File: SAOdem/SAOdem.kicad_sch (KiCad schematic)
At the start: 1 part, among them U1 SI3018

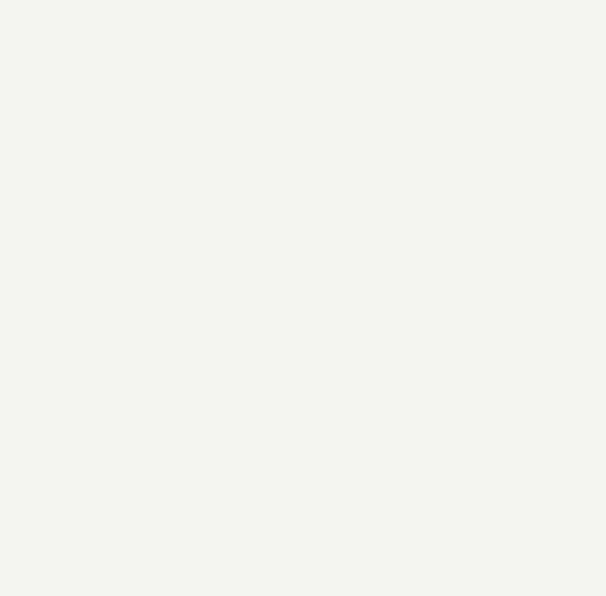
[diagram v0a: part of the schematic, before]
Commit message: Adding Modem chip symbol
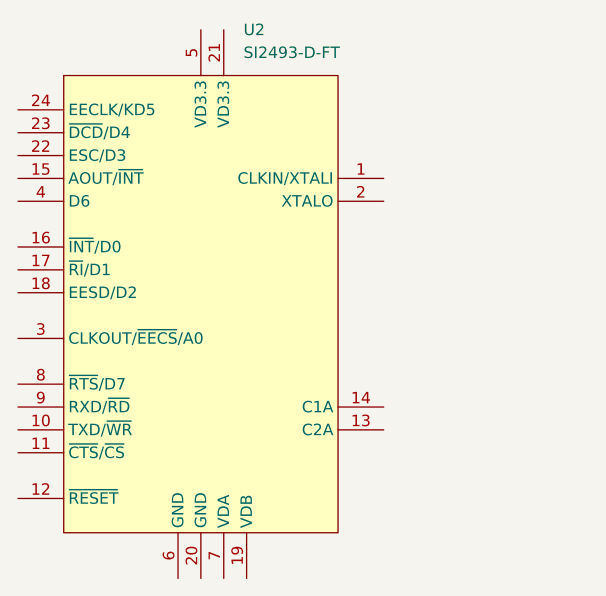
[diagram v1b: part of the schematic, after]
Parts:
- added U2: SI2493-D-FT, Package_SO:TSSOP-24_4.4x6.5mm_P0.5mm, symbol SAOdem:SI2493-D-FT
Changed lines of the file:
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@@
 	(paper "USLetter")
+	(symbol
+		(lib_id "SAOdem:SI2493-D-FT")
+		(at 121.92 82.55 0)
+		(unit 1)
+		(exclude_from_sim no)
+		(in_bom yes)
+		(on_board yes)
+		(dnp no)
+		(fields_autoplaced yes)
+		(property "Reference" "U2"
+			(at 126.6541 52.07 0)
+			(effects
+				(font
+					(size 1.27 1.27)
+				)
+				(justify left)
+			)
+		)
+		(property "Value" "SI2493-D-FT"
+			(at 126.6541 54.61 0)
+			(effects
+				(font
+					(size 1.27 1.27)
+				)
+				(justify left)
+			)
+		)
+		(property "Footprint" "Package_SO:TSSOP-24_4.4x6.5mm_P0.5mm"
+			(at 121.92 82.55 0)
+			(effects
+				(font
+					(size 1.27 1.27)
+				)
+				(hide yes)
+			)
+		)
+		(property "Datasheet" "https://www.skyworksinc.com/-/media/SkyWorks/SL/documents/public/data-sheets/Si2493D.pdf"
+			(at 121.92 82.55 0)
+			(effects
+				(font
+					(size 1.27 1.27)
+				)
+				(hide yes)
+			)
+		)
+		(property "Description" ""
+			(at 121.92 82.55 0)
+			(effects
+				(font
+					(size 1.27 1.27)
+				)
+				(hide yes)
+			)
+		)
+		(pin "23"
+		)
+		(pin "1"
+		)
+		(pin "10"
+		)
+		(pin "9"
+		)
+		(pin "17"
+		)
+		(pin "3"
+		)
+		(pin "20"
+		)
+		(pin "14"
+		)
+		(pin "15"
+		)
+		(pin "2"
+		)
+		(pin "22"
+		)
+		(pin "6"
+		)
+		(pin "24"
+		)
+		(pin "21"
+		)
+		(pin "19"
+		)
+		(pin "5"
+		)
+		(pin "7"
+		)
+		(pin "13"
+		)
+		(pin "11"
+		)
+		(pin "18"
+		)
+		(pin "8"
+		)
+		(pin "12"
+		)
+		(pin "4"
+		)
+		(pin "16"
+		)
+		(instances
+			(project ""
+				(path "/a378d284-dbde-4dc9-b578-a5e5f353675f"
+					(reference "U2")
+					(unit 1)
+				)
+			)
+		)
+	)
 	(symbol
 		(lib_id "SAOdem:SI3018")

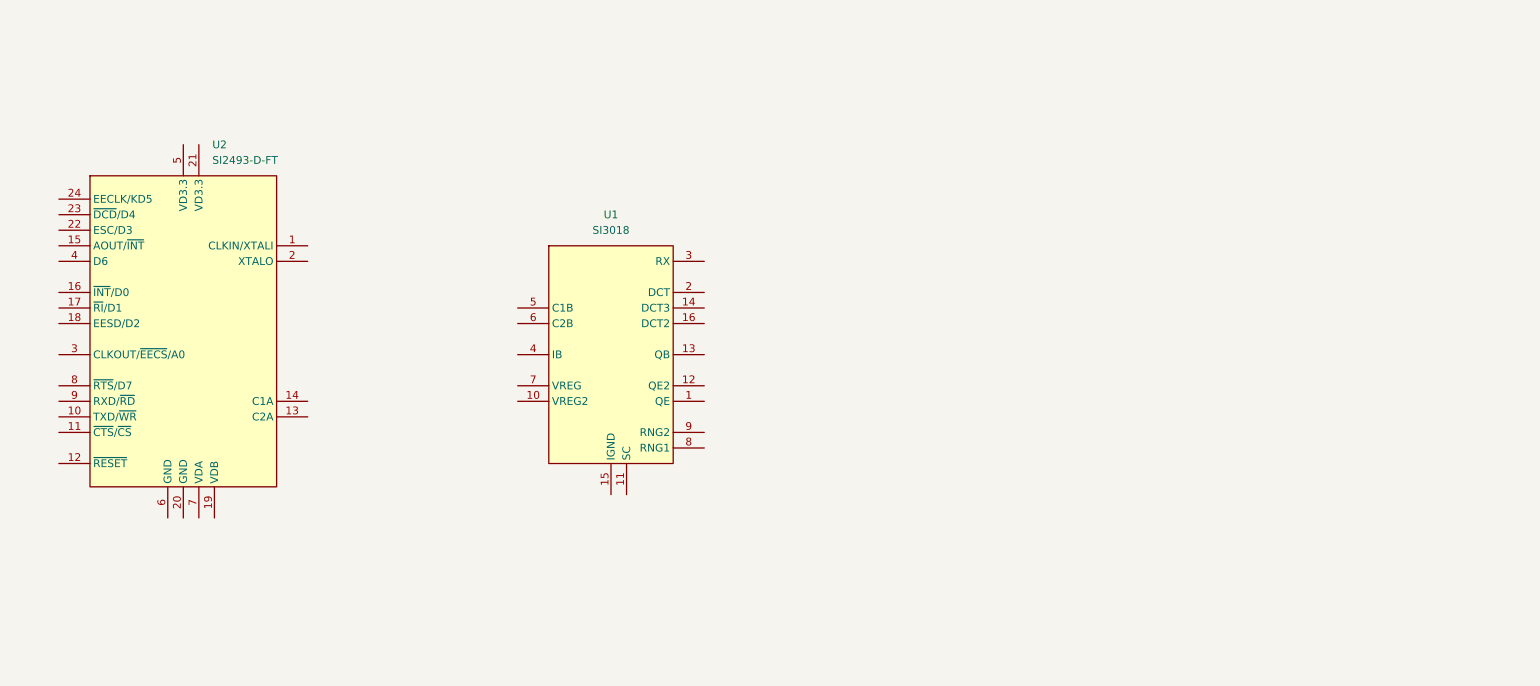
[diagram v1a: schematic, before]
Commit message: Started adding schematic for DAA
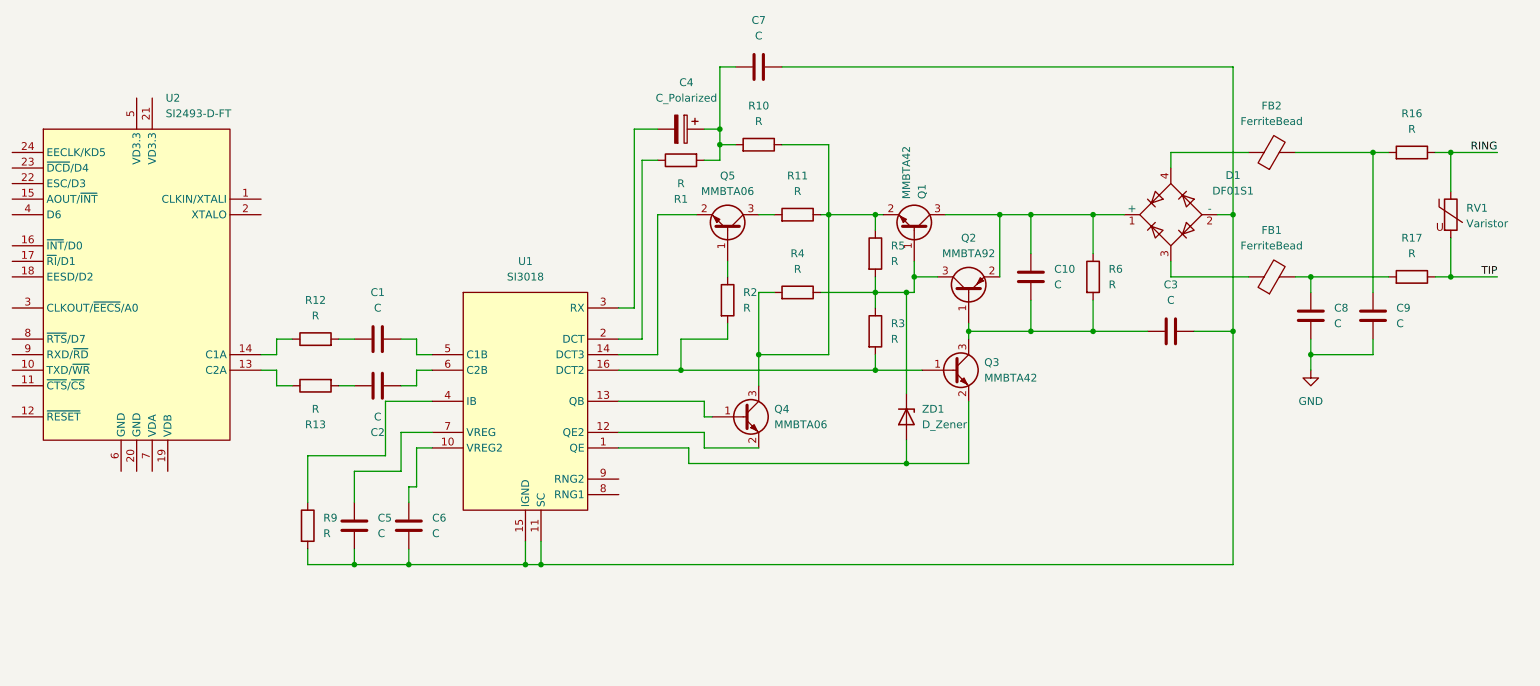
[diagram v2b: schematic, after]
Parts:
- added C1, C10, C2, C3, C5, C6, C7, C8, C9: C, symbol Device:C
- added C4: C_Polarized, symbol Device:C_Polarized
- added D1: DF01S1, Diode_SMD:Diode_Bridge_OnSemi_SDIP-4L, symbol Diode_Bridge:DF01S1
- added FB1, FB2: FerriteBead, symbol Device:FerriteBead
- added Q1, Q3: MMBTA42, Package_TO_SOT_SMD:SOT-23, symbol Transistor_BJT:MMBTA42
- added Q2: MMBTA92, Package_TO_SOT_SMD:SOT-23, symbol Transistor_BJT:MMBTA92
- added Q4, Q5: MMBTA06, Package_TO_SOT_SMD:SOT-23, symbol Transistor_BJT:MMBTA06
- added R1, R10, R11, R12, R13, R16, R17, R2, R3, R4, R5, R6, R9: R, symbol Device:R
- added RV1: Varistor, symbol Device:Varistor
- added ZD1: D_Zener, symbol Device:D_Zener
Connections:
- net at U2.13 (C2A): now also R13.1
- net at U2.14 (C1A): now also R12.1
- net at U1.1 (QE): now also Q3.2 (E), ZD1.2 (A)
- net at U1.10 (VREG2): now also C6.1
- net at U1.11 (SC): now also U1.15 (IGND), C3.1, C5.2, C6.2, C7.2, D1.2 (-), R9.2
- net at U1.12 (QE2): now also Q4.2 (E)
- net at U1.13 (QB): now also Q4.1 (B)
- net at U1.14 (DCT3): now also Q5.2 (E)
- net at U1.16 (DCT2): now also Q3.1 (B), R2.2, R3.2
- net at U1.2 (DCT): now also R1.1
- net at U1.3 (RX): now also C4.2
- net at U1.4 (IB): now also R9.1
- net at U1.5 (C1B): now also C1.2
- net at U1.6 (C2B): now also C2.1
- net at U1.7 (VREG): now also C5.1
- new net: Q1.1 (B), Q2.3 (C), R3.1, R4.1, R5.2, ZD1.1 (K)
- new net: Q1.2 (E), Q4.3 (C), R10.1, R11.1, R4.2, R5.1
- new net: C8.2, FB1.2, R17.2
- new net: C4.1, C7.1, R1.2, R10.2
- new net: C10.1, C3.2, Q2.1 (B), Q3.3 (C), R6.2
- new net: C10.2, D1.1 (+), Q1.3 (C), Q2.2 (E), R6.1
- new net: C1.1, R12.2
- new net: C9.2, FB2.2, R16.2
- new net: Q5.1 (B), R2.1
- new net: D1.3, FB1.1
- new net: C2.2, R13.2
- new net: D1.4, FB2.1
- new net: Q5.3 (C), R11.2
- new net GND: C8.1, C9.1
- new net RING: R16.1, RV1.1
- new net TIP: R17.1, RV1.2
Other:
- moved on the sheet: U1, U2

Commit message: Finishing DAA schematic, and adding documentation
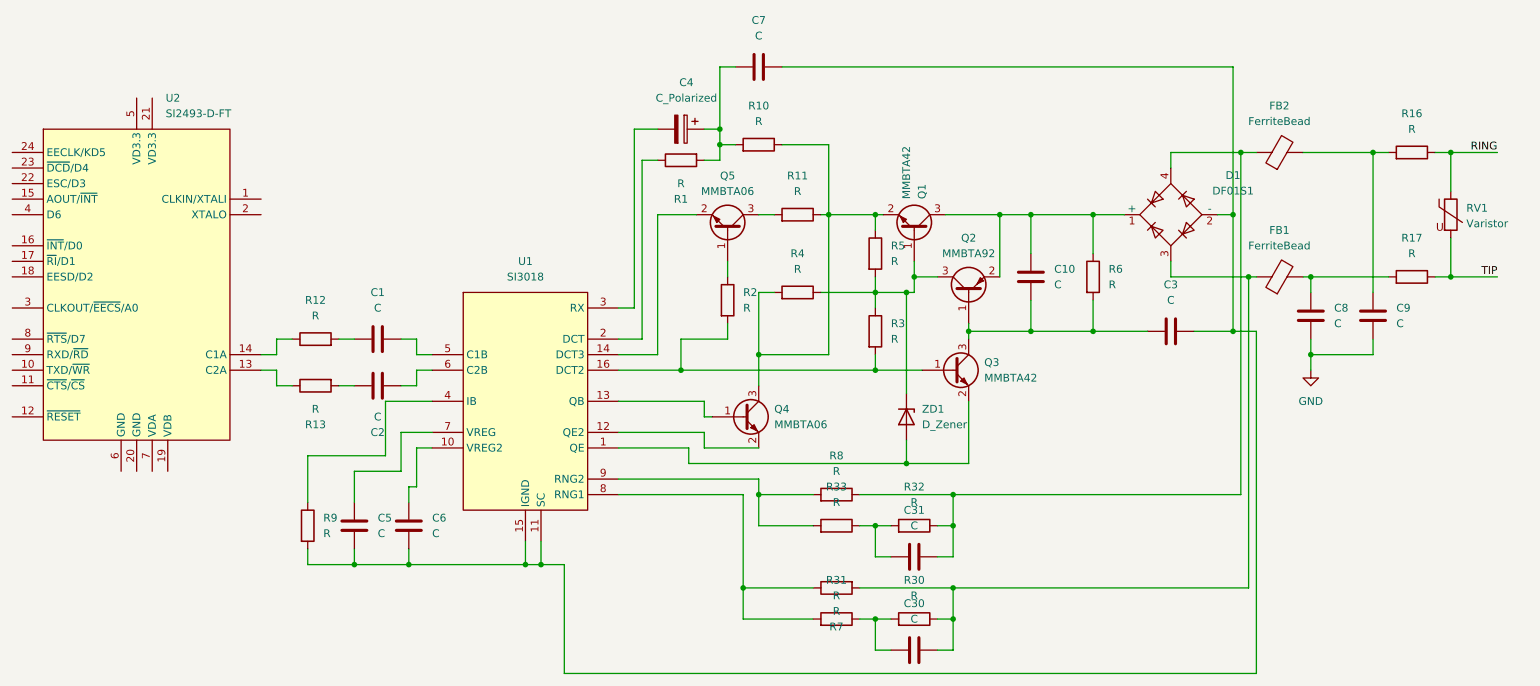
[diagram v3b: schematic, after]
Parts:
- added C30, C31: C, symbol Device:C
- added R30, R31, R32, R33, R7, R8: R, symbol Device:R
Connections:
- net at D1.3, FB1.1: now also C30.2, R30.1, R7.2
- net at D1.4, FB2.1: now also C31.2, R32.1, R8.1
- net at U1.8 (RNG1): now also R31.2, R7.1
- net at U1.9 (RNG2): now also R33.2, R8.2
- new net: C30.1, R30.2, R31.1
- new net: C31.1, R32.2, R33.1
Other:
- moved on the sheet: FB1, FB2
